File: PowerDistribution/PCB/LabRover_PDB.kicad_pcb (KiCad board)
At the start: 4 copper layers, 79 x 80 mm, 71 parts, among them IC1 TLV1117LV33DCYR, IC10 SI4162DY-T1-GE3, IC11 ESP32-S3-WROOM-1U-N8, IC2 LM75BDP,118, IC3 INA219AIDR, IC4 SN74LVC1G08DBVR, IC5 SI4162DY-T1-GE3, IC6 SI4162DY-T1-GE3, IC7 SI4162DY-T1-GE3, IC8 SI4162DY-T1-GE3, IC9 ADS1015BQDGSRQ1, J1 Conn_01x02, J10 USB_C_Receptacle_USB2.0_16P, J2 Conn_01x02, J3 Conn_01x02, J4 Conn_01x02, J5 Conn_01x02, J6 Conn_01x02, J7 Conn_01x02, J8 Conn_01x02, Q1 BSS84, SW1 SW_Push, SW2 SW_Push, U2 USBLC6-2SC6

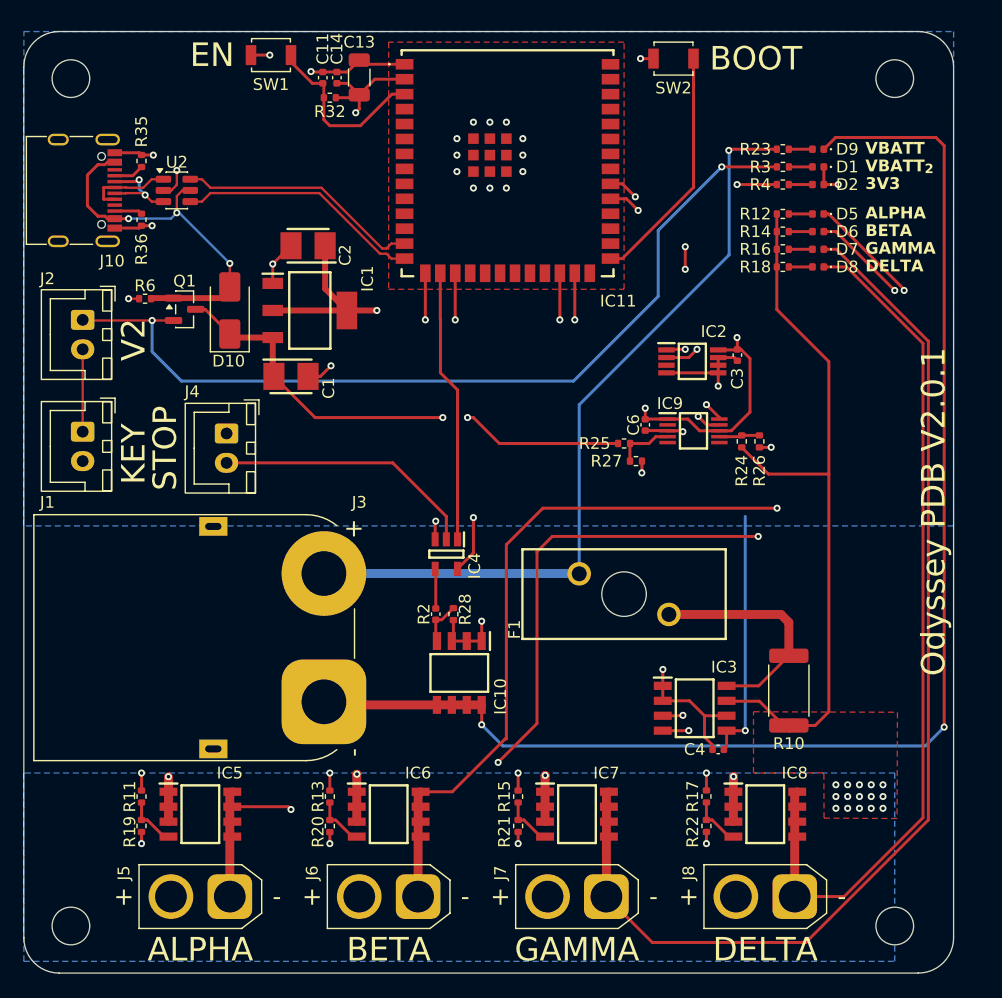
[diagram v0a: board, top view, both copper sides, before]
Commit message: Adds PDB v2.0
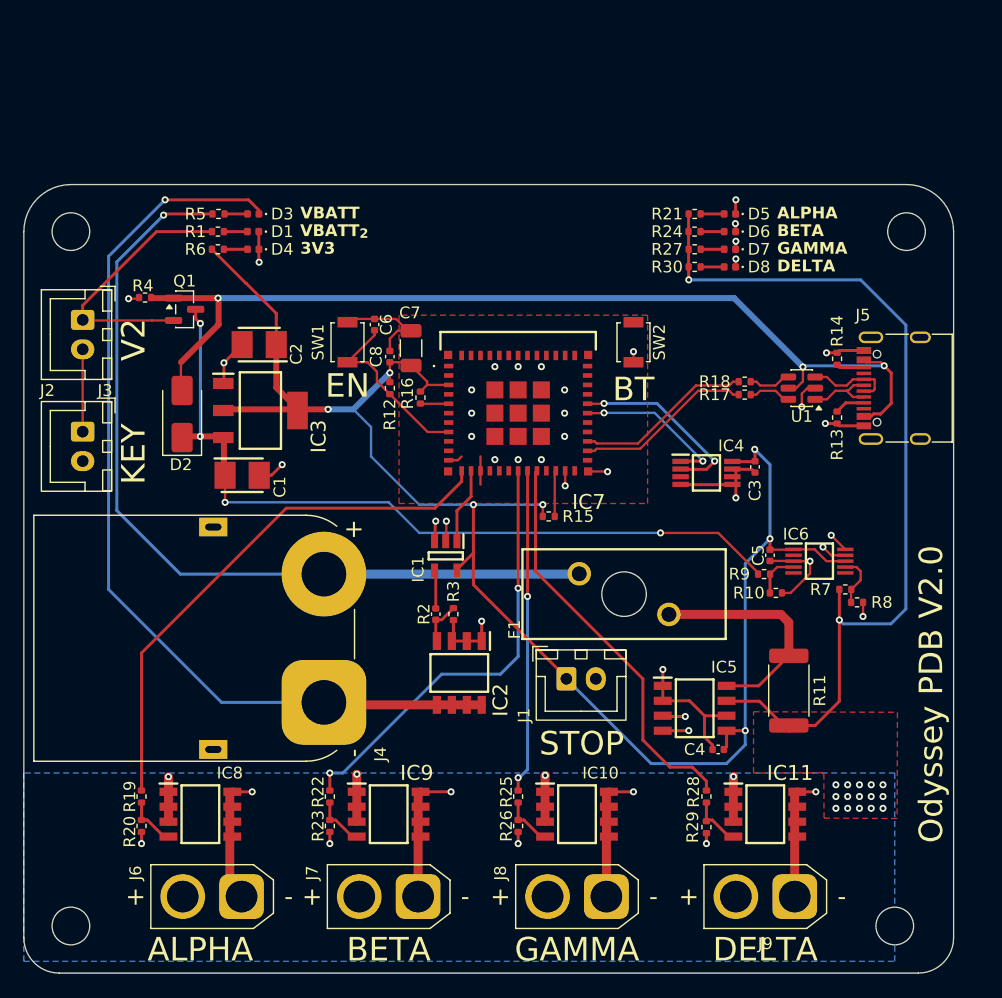
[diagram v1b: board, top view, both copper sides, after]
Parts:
- removed C11: 1u, Capacitor_SMD:C_0402_1005Metric
- removed C13: 22u, Capacitor_SMD:C_1206_3216Metric
- removed C14: 100n, Capacitor_SMD:C_0402_1005Metric
- removed D10: SS12, Diode_SMD:D_SMA
- removed D9: GREEN, LED_SMD:LED_0402_1005Metric
- removed J10: USB_C_Receptacle_USB2.0_16P, Connector_USB:USB_C_Receptacle_G-Switch_GT-USB-7010ASV
- removed R32: 10k, Resistor_SMD:R_0402_1005Metric
- removed R35, R36: 5K1, Resistor_SMD:R_0402_1005Metric
- removed U2: USBLC6-2SC6, Package_TO_SOT_SMD:SOT-23-6
- added C5: 1u, Capacitor_SMD:C_0402_1005Metric, F.Cu at (171.4, 99.5)
- added C7: 22u, Capacitor_SMD:C_1206_3216Metric, F.Cu at (140.9, 81.9)
- added C8: 100n, Capacitor_SMD:C_0402_1005Metric, F.Cu at (139.1, 82.6)
- added D3: GREEN, LED_SMD:LED_0402_1005Metric, F.Cu at (127.5, 70.5)
- added D4: GREEN, LED_SMD:LED_0402_1005Metric, F.Cu at (127.5, 73.5)
- added J9: Conn_01x02, Connector_AMASS:AMASS_XT30U-M_1x02_P5.0mm_Vertical, F.Cu at (173.5, 128.5)
- added R1: 1kR, Resistor_SMD:R_0402_1005Metric, F.Cu at (124.5, 72.0)
- added R29: 10k, Resistor_SMD:R_0402_1005Metric, F.Cu at (166.0, 122.6)
- added R30: 470, Resistor_SMD:R_0402_1005Metric, F.Cu at (165.0, 75.0)
- added R5: 2.4k, Resistor_SMD:R_0402_1005Metric, F.Cu at (124.5, 70.5)
- added R7: 560k, Resistor_SMD:R_0402_1005Metric, F.Cu at (177.8, 102.4)
- added R8: 100k, Resistor_SMD:R_0402_1005Metric, F.Cu at (178.8, 103.5)
- added R9: 5.1k, Resistor_SMD:R_0402_1005Metric, F.Cu at (170.9, 101.1)
- added U1: USBLC6-2SC6, Package_TO_SOT_SMD:SOT-23-6, F.Cu at (174.1, 85.3)
- D2: value GREEN -> SS12; footprint LED_SMD:LED_0402_1005Metric -> Diode_SMD:D_SMA
- IC1: value TLV1117LV33DCYR -> SN74LVC1G08DBVR; footprint Footprints:SOT230P700X180-4N -> Footprints:SOT95P280X145-5N
- IC11: value ESP32-S3-WROOM-1U-N8 -> SI4162DY-T1-GE3; footprint Footprints:ESP32S3WROOM1UN8 -> Footprints:SOIC127P600X175-8N
- IC2: value LM75BDP,118 -> SI4162DY-T1-GE3; footprint Footprints:SOP65P490X110-8N -> Footprints:SOIC127P600X175-8N
- IC3: value INA219AIDR -> TLV1117LV33DCYR; footprint Footprints:SOIC127P600X175-8N -> Footprints:SOT230P700X180-4N
- IC4: value SN74LVC1G08DBVR -> LM75BDP,118; footprint Footprints:SOT95P280X145-5N -> Footprints:SOP65P490X110-8N
- IC5: value SI4162DY-T1-GE3 -> INA219AIDR
- IC6: value SI4162DY-T1-GE3 -> ADS1015BQDGSRQ1; footprint Footprints:SOIC127P600X175-8N -> Footprints:SOP50P490X110-10N
- IC7: value SI4162DY-T1-GE3 -> ESP32-C3-MINI-1U-N4X; footprint Footprints:SOIC127P600X175-8N -> Footprints:ESP32C3MINI1UN4X
- IC9: value ADS1015BQDGSRQ1 -> SI4162DY-T1-GE3; footprint Footprints:SOP50P490X110-10N -> Footprints:SOIC127P600X175-8N
- J3: footprint Connector_AMASS:AMASS_XT90PW-M_1x02_P10.90mm_Horizontal -> Connector_JST:JST_XH_B2B-XH-A_1x02_P2.50mm_Vertical
- J4: footprint Connector_JST:JST_XH_B2B-XH-A_1x02_P2.50mm_Vertical -> Connector_AMASS:AMASS_XT90PW-M_1x02_P10.90mm_Horizontal
- J5: value Conn_01x02 -> USB_C_Receptacle_USB2.0_16P; footprint Connector_AMASS:AMASS_XT30U-M_1x02_P5.0mm_Vertical -> Connector_USB:USB_C_Receptacle_G-Switch_GT-USB-7010ASV
- R10: value 0.01 -> 10k; footprint Resistor_SMD:R_2512_6332Metric -> Resistor_SMD:R_0402_1005Metric
- R11: value 100 -> 0.01; footprint Resistor_SMD:R_0402_1005Metric -> Resistor_SMD:R_2512_6332Metric
- R12, R16: value 470 -> 10k
- R13: value 100 -> 5K1
- R14: value 470 -> 5K1
- R15: value 100 -> 10k
- R17: value 100 -> 22
- R18: value 470 -> 22
- R19, R22, R28: value 10k -> 100
- R21, R27: value 10k -> 470
- R23: value 2.4k -> 10k
- R24: value 560k -> 470
- R25: value 5.1k -> 100
- R26: value 100k -> 10k
- R3: value 1kR -> 10k
- R4: value 600 -> 10kR
- R6: value 10kR -> 600
- moved J5 72.0 mm to (183.1, 85.3), turned to 90 degrees
- moved R23 69.2 mm to (134.0, 122.5), turned to 90 degrees
- moved IC11 59.5 mm to (171.0, 121.5)
- moved D2 57.5 mm to (121.5, 87.5), turned to 90 degrees
- moved R11 55.7 mm to (173.0, 111.0), turned to -90 degrees
- moved R4 55.0 mm to (118.3, 77.6), turned to 0 degrees
- moved R21 54.1 mm to (165.0, 70.5), turned to 180 degrees
- moved R13 53.8 mm to (177.1, 87.8), turned to -90 degrees
- moved D1 48.3 mm to (127.5, 72.0)
- moved IC8 48.0 mm to (123.0, 121.5)
- moved R3 47.2 mm to (144.5, 104.5), turned to 90 degrees
- moved J1 46.2 mm to (154.1, 110.0), turned to 0 degrees
- moved IC3 44.7 mm to (128.1, 87.2)
- moved IC5 43.0 mm to (165.0, 112.5)
- moved IC6 42.4 mm to (175.6, 100.0)
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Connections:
- C6 pad 1: +3.3V -> /ESP32_C3/RST
- D2 pad 1: GND -> /Power_Protection/VBATT_{2}Read
- D2 pad 2: Net-(D2-A) -> /ESP32_C3/5V
- F1 pad 1: Net-(J3-Pin_2) -> Net-(J4-Pin_2)
- IC1 pad 1: GND -> /ESP32_C3/GPIO1
- IC1 pad 2: +3.3V -> Net-(IC1-B)
- IC1 pad 3: /Power_Protection/VBATT_{2}Read -> GND
- IC1 pad 4: +3.3V -> Net-(IC1-Y)
- IC10 pad 5: Net-(D9-K) -> Net-(D7-K)
- IC10 pad 6: Net-(D9-K) -> Net-(D7-K)
- IC10 pad 7: Net-(D9-K) -> Net-(D7-K)
- IC10 pad 8: Net-(D9-K) -> Net-(D7-K)
- IC11 pad 2: +3.3V -> GND
- IC11 pad 3: /uC/RST -> GND
- IC11 pad 4: /uC/GPIO4 -> Net-(IC11-G)
- IC11 pad 5: /uC/GPIO5 -> Net-(D8-K)
- IC11 pad 6: /uC/GPIO6 -> Net-(D8-K)
- IC11 pad 7: /uC/GPIO7 -> Net-(D8-K)
- IC11 pad 8: /uC/GPIO15 -> Net-(D8-K)
- IC2 pad 1: /Sensors/SDA -> GND
- IC2 pad 2: /Sensors/SCL -> GND
- IC2 pad 3: unconnected-(IC2-OS-Pad3) -> GND
- IC2 pad 4: GND -> Net-(IC2-G)
- IC2 pad 5: GND -> Net-(D3-K)
- IC2 pad 6: GND -> Net-(D3-K)
- IC2 pad 7: GND -> Net-(D3-K)
- IC2 pad 8: +3.3V -> Net-(D3-K)
- IC3 pad 2: GND -> +3.3V
- IC3 pad 3: /Sensors/SDA -> /Power_Protection/VBATT_{2}Read
- IC3 pad 4: /Sensors/SCL -> +3.3V
- IC4 pad 1: /Power_Protection/FET_{Switch Main} -> /ESP32_C3/GPIO20
- IC4 pad 2: Net-(IC4-B) -> /ESP32_C3/GPIO21
- IC4 pad 3: GND -> unconnected-(IC4-OS-Pad3)
- IC4 pad 4: Net-(IC4-Y) -> GND
- IC4 pad 5: +3.3V -> GND
- IC5 pad 3: GND -> /ESP32_C3/GPIO20
- IC5 pad 4: Net-(IC5-G) -> /ESP32_C3/GPIO21
- IC5 pad 5: Net-(D5-K) -> +3.3V
- IC5 pad 6: Net-(D5-K) -> GND
- IC5 pad 7: Net-(D5-K) -> +BATT_SENSED
- IC5 pad 8: Net-(D5-K) -> /Sensors/IN+
- IC6 pad 1: GND -> +3.3V
- IC6 pad 2: GND -> unconnected-(IC6-ALERT/RDY-Pad2)
- IC6 pad 4: Net-(IC6-G) -> /Sensors/AIN0
- IC6 pad 5: Net-(D6-K) -> unconnected-(IC6-AIN1-Pad5)
- IC6 pad 6: Net-(D6-K) -> unconnected-(IC6-AIN2-Pad6)
- IC6 pad 7: Net-(D6-K) -> /Sensors/AIN3
- IC6 pad 8: Net-(D6-K) -> +3.3V
- IC7 pad 3: GND -> +3.3V
- IC7 pad 4: Net-(IC7-G) -> unconnected-(IC7-NC_1-Pad4)
- IC7 pad 5: Net-(D7-K) -> /ESP32_C3/GPIO2
- IC7 pad 6: Net-(D7-K) -> /ESP32_C3/GPIO3
- IC7 pad 7: Net-(D7-K) -> unconnected-(IC7-NC_2-Pad7)
- IC7 pad 8: Net-(D7-K) -> /ESP32_C3/RST
- IC8 pad 5: Net-(D8-K) -> Net-(D5-K)
- IC8 pad 6: Net-(D8-K) -> Net-(D5-K)
- IC8 pad 7: Net-(D8-K) -> Net-(D5-K)
- IC8 pad 8: Net-(D8-K) -> Net-(D5-K)
- IC9 pad 1: +3.3V -> GND
- IC9 pad 2: unconnected-(IC9-ALERT/RDY-Pad2) -> GND
- IC9 pad 4: /Sensors/AIN0 -> Net-(IC9-G)
- IC9 pad 5: unconnected-(IC9-AIN1-Pad5) -> Net-(D6-K)
- IC9 pad 6: unconnected-(IC9-AIN2-Pad6) -> Net-(D6-K)
- IC9 pad 7: /Sensors/AIN3 -> Net-(D6-K)
- IC9 pad 8: +3.3V -> Net-(D6-K)
- J1 pad 1: Net-(J1-Pin_1) -> +3.3V
- J1 pad 2: GND -> Net-(IC1-B)
- J2 pad 1: +VBATT_{2} -> Net-(J2-Pin_1)
- J2 pad 2: Net-(J1-Pin_1) -> GND
- J3 pad 1: Net-(D9-K) -> +VBATT_{2}
- J3 pad 2: Net-(J3-Pin_2) -> Net-(J2-Pin_1)
- J4 pad 1: +3.3V -> Net-(D3-K)
- J4 pad 2: Net-(IC4-B) -> Net-(J4-Pin_2)
- J6 pad 1: Net-(D6-K) -> Net-(D5-K)
- J7 pad 1: Net-(D7-K) -> Net-(D6-K)
- J8 pad 1: Net-(D8-K) -> Net-(D7-K)
- Q1 pad 1: /Power_Protection/5V -> /ESP32_C3/5V
- R10 pad 1: /Sensors/IN+ -> /Sensors/AIN0
- R10 pad 2: +BATT_SENSED -> GND
- R11 pad 1: Net-(IC5-G) -> /Sensors/IN+
- R11 pad 2: /POWER_OUT/FET_{Switch_} -> +BATT_SENSED
- R12 pad 1: Net-(D5-A) -> /ESP32_C3/RST
- R12 pad 2: +BATT_SENSED -> +3.3V
- R13 pad 1: Net-(IC6-G) -> Net-(J5-CC1)
- R13 pad 2: /POWER_OUT1/FET_{Switch_} -> GND
- R14 pad 1: Net-(D6-A) -> GND
- R14 pad 2: +BATT_SENSED -> Net-(J5-CC2)
- R15 pad 1: Net-(IC7-G) -> +3.3V
- R15 pad 2: /POWER_OUT2/FET_{Switch_} -> /ESP32_C3/GPIO8
- R16 pad 1: Net-(D7-A) -> +3.3V
- R16 pad 2: +BATT_SENSED -> /ESP32_C3/GPIO2
- R17 pad 1: Net-(IC8-G) -> /ESP32_C3/DR-
- R17 pad 2: /POWER_OUT3/FET_{Switch_} -> /ESP32_C3/D-
- R18 pad 1: Net-(D8-A) -> /ESP32_C3/DR+
- R18 pad 2: +BATT_SENSED -> /ESP32_C3/D+
- R19 pad 1: GND -> Net-(IC8-G)
- R19 pad 2: Net-(IC5-G) -> /ESP32_C3/GPIO0
- R2 pad 1: Net-(IC4-Y) -> Net-(IC1-Y)
- R2 pad 2: Net-(IC10-G) -> Net-(IC2-G)
- R20 pad 2: Net-(IC6-G) -> Net-(IC8-G)
- R21 pad 1: GND -> Net-(D5-A)
- R21 pad 2: Net-(IC7-G) -> +BATT_SENSED
- R22 pad 1: GND -> Net-(IC9-G)
- R22 pad 2: Net-(IC8-G) -> /ESP32_C3/GPIO4
- R23 pad 1: Net-(D9-A) -> GND
- R23 pad 2: Net-(J3-Pin_2) -> Net-(IC9-G)
- R24 pad 1: +BATT_SENSED -> Net-(D6-A)
- R24 pad 2: /Sensors/AIN3 -> +BATT_SENSED
- R25 pad 1: /Power_Protection/VBATT_{2}Read -> Net-(IC10-G)
- R25 pad 2: /Sensors/AIN0 -> /ESP32_C3/GPIO5
- R26 pad 1: /Sensors/AIN3 -> GND
- R26 pad 2: GND -> Net-(IC10-G)
- R27 pad 1: /Sensors/AIN0 -> Net-(D7-A)
- R27 pad 2: GND -> +BATT_SENSED
- R28 pad 1: GND -> Net-(IC11-G)
- R28 pad 2: Net-(IC10-G) -> /ESP32_C3/GPIO6
- R3 pad 1: Net-(D1-A) -> GND
- R3 pad 2: +VBATT_{2} -> Net-(IC2-G)
- R4 pad 1: Net-(D2-A) -> GND
- R4 pad 2: +3.3V -> /ESP32_C3/5V
- R6 pad 1: GND -> Net-(D4-A)
- R6 pad 2: /Power_Protection/5V -> +3.3V
- SW1 pad 1: /uC/RST -> /ESP32_C3/RST
- SW2 pad 1: /uC/BOOT -> /ESP32_C3/BOOT
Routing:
- net Net-(D9-K): track 116.4 -> 0.00 mm, vias 2 -> 0
- net /ESP32_C3/5V: track 0.00 -> 84.5 mm, vias 0 -> 3
- net Net-(D3-K): track 0.00 -> 79.7 mm, vias 0 -> 1
- net Net-(J4-Pin_2): track 0.00 -> 72.4 mm, vias 0 -> 1
- net Net-(J3-Pin_2): track 67.1 -> 0.00 mm, vias 1 -> 0
- net +3.3V: track 74.9 -> 141.5 mm
- net /ESP32_C3/GPIO21: track 0.00 -> 64.4 mm, vias 0 -> 4
- net /ESP32_C3/GPIO20: track 0.00 -> 61.8 mm, vias 0 -> 4
- net /Sensors/SCL: track 56.8 -> 0.00 mm, vias 4 -> 0
- net /Sensors/SDA: track 54.8 -> 0.00 mm, vias 6 -> 0
- net /POWER_OUT/FET_{Switch_}: track 54.0 -> 0.00 mm, vias 2 -> 0
- net /POWER_OUT3/FET_{Switch_}: track 52.9 -> 0.00 mm, vias 2 -> 0
- net +VBATT_{2}: track 75.3 -> 22.5 mm, vias 2 -> 0
- net /POWER_OUT1/FET_{Switch_}: track 50.3 -> 0.00 mm, vias 2 -> 0
- net /ESP32_C3/GPIO0: track 0.00 -> 45.8 mm
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- removed copper zone on B.Cu, net +3.3V
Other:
- board size 79 x 80 mm -> 79 x 67 mm
- board text added: "BT"
- board text added: "Odyssey PDB V2.0"
- board text removed: "BOOT"
- board text removed: "Odyssey PDB V2.0.1"
